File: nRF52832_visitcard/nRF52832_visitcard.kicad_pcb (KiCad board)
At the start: 4 copper layers, 91 x 50 mm, 67 parts, among them J1 Programming, J2 UART, SW1 SW_Push, Y1 32 MHz

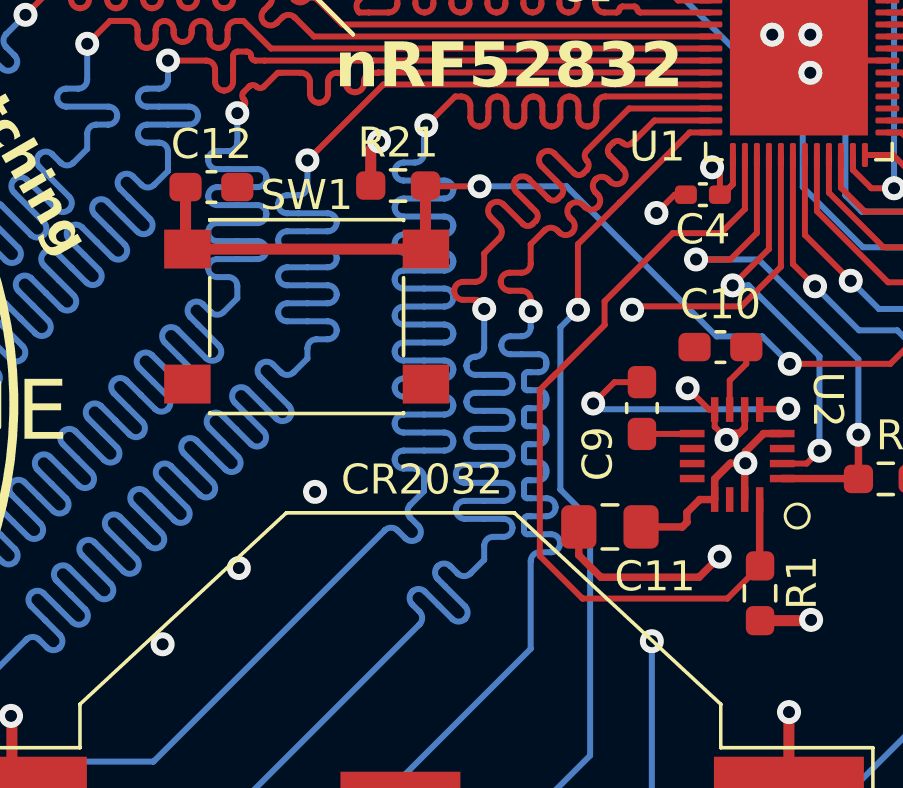
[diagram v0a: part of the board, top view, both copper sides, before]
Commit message: LCSC added to another component
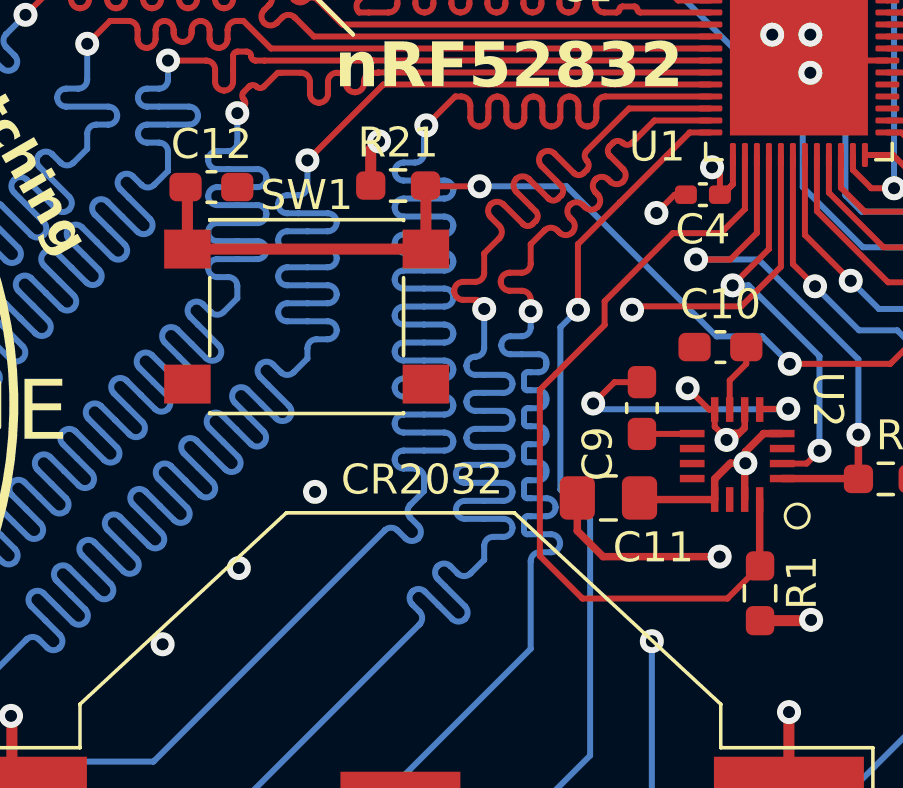
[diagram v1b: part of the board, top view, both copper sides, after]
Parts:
- moved C11 0.97 mm to (162.2, 108.2)
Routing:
- net VDD: track 43.7 -> 43.2 mm

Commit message: Board layout fix
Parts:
- removed the   at (116.9, 114.9)
- moved R2 8.53 mm to (163.3, 104.8), turned to 135 degrees
- moved R1 8.48 mm to (160.7, 105.9), turned to 180 degrees
- moved C9 8.20 mm to (171.1, 107.5)
- moved C10 6.45 mm to (169.4, 108.5), turned to -90 degrees
- moved C11 0.90 mm to (162.9, 108.7), turned to -90 degrees
- moved U2 0.68 mm to (166.3, 107.4), turned to 0 degrees
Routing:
- net /SCL: track 27.7 -> 16.0 mm
- net /SDA: track 18.3 -> 11.6 mm, vias 2 -> 0
- net /SETC: track 9.47 -> 3.23 mm, vias 2 -> 0
- net /SETP: track 1.68 -> 6.86 mm
- net GND: track 47.5 -> 43.7 mm, vias 91 -> 90
- net /D12: track 118.4 -> 115.8 mm
- net VDD: track 43.2 -> 44.3 mm
- net Net-(U2-C1): track 2.31 -> 1.50 mm
- net /PB: track 39.7 -> 39.2 mm
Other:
- board text removed: "+38766170888"
- board text removed: "Co-Founder"
- board text removed: "damjan.prerad@indigoingenium.ba"
- board text removed: "https://indigoingenium.ba"

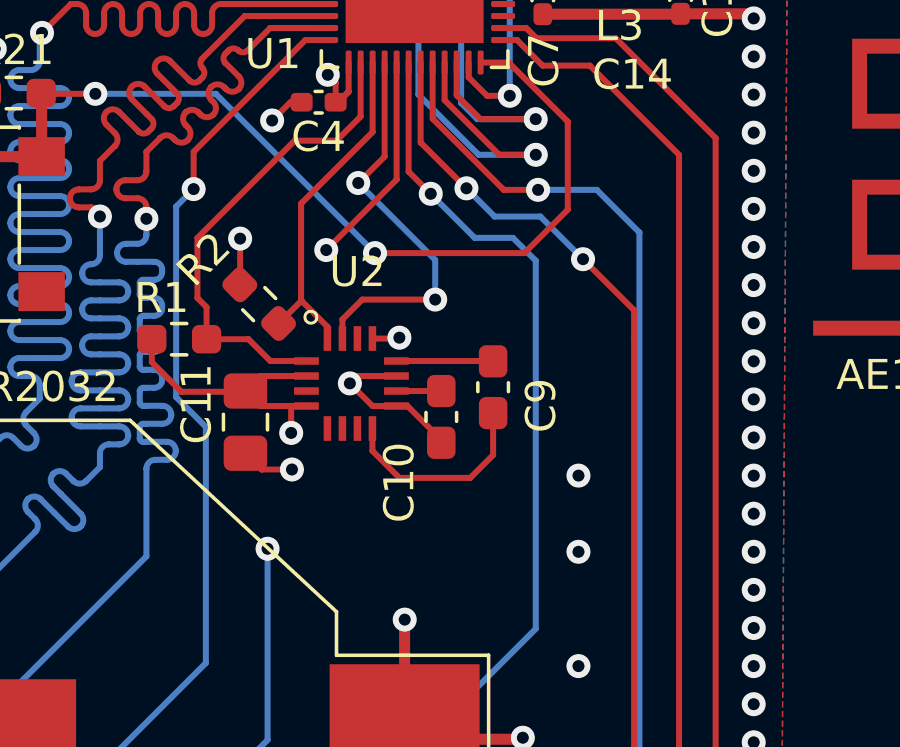
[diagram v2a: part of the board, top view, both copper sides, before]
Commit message: Using QMC5833L instead of HMC5883L
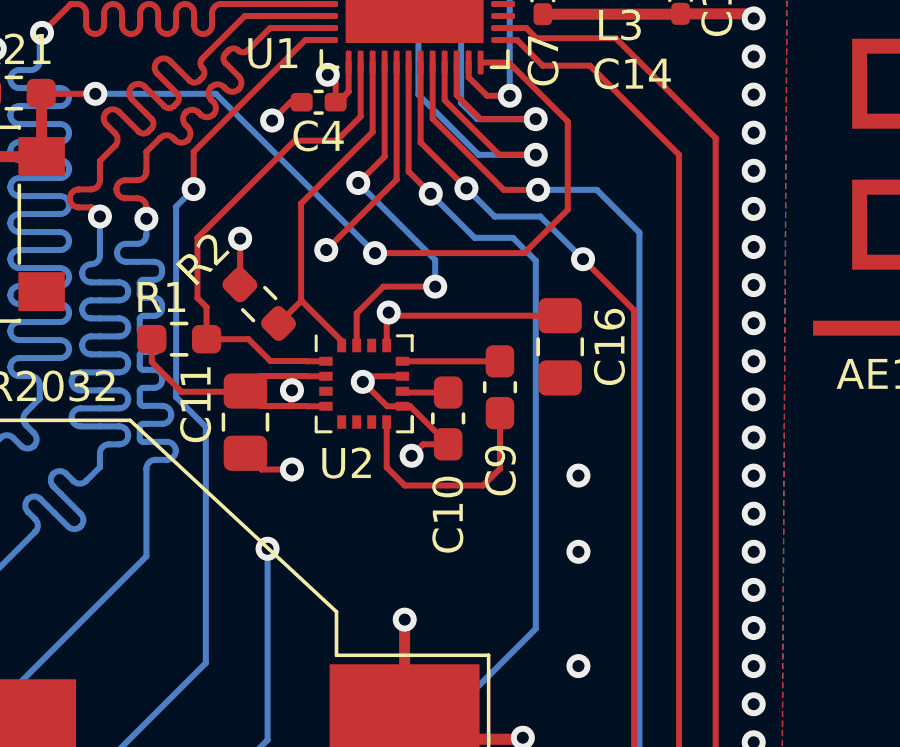
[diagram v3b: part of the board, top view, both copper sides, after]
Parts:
- added C16: 100n, Capacitor_SMD:C_0805_2012Metric_Pad1.18x1.45mm_HandSolder, F.Cu at (173.4, 106.2)
- U2: footprint HMC5883L:HMC5883L -> Package_LGA:LGA-16_3x3mm_P0.5mm
- moved U2 0.51 mm to (166.8, 107.4)
- moved C10 0.23 mm to (169.6, 108.6)
- moved C9 0.23 mm to (171.4, 107.5)
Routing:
- net VDD: track 44.3 -> 51.7 mm
- net GND: track 43.7 -> 44.6 mm, vias 90 -> 91
- net /SETP: track 6.86 -> 7.62 mm
- net /SCL: track 16.0 -> 16.7 mm
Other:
- board text added: "Bluetooth compass"
- board text added: "damjanovmail@gmail.com"
- board text removed: "INDIGO INGENUM"

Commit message: PCB details - Rotated battery holder in 3D view - Silkscreen fix
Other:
- board text added: "UART"
- board text removed: "Linux Bare-Metal"
- board text removed: "Python C / C++"
- board text removed: "Software and firmawre development PCB design and layout"
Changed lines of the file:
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@@
 (kicad_pcb (version 20221018) (generator pcbnew)
   (general
-    (thickness 0.19)
+    (thickness 1.5)
   )
   (paper "A4")
@@
       (layer "F.Mask" (type "Top Solder Mask") (thickness 0.01))
       (layer "F.Cu" (type "copper") (thickness 0.035))
-      (layer "dielectric 1" (type "prepreg") (thickness 0.01) (material "FR4") (epsilon_r 4.5) (loss_tangent 0.02))
+      (layer "dielectric 1" (type "prepreg") (thickness 0.1) (material "FR4") (epsilon_r 4.5) (loss_tangent 0.02))
       (layer "In1.Cu" (type "copper") (thickness 0.035))
-      (layer "dielectric 2" (type "core") (thickness 0.01) (material "FR4") (epsilon_r 4.5) (loss_tangent 0.02))
+      (layer "dielectric 2" (type "core") (thickness 1.14) (material "FR4") (epsilon_r 4.5) (loss_tangent 0.02))
       (layer "In2.Cu" (type "copper") (thickness 0.035))
-      (layer "dielectric 3" (type "prepreg") (thickness 0.01) (material "FR4") (epsilon_r 4.5) (loss_tangent 0.02))
+      (layer "dielectric 3" (type "prepreg") (thickness 0.1) (material "FR4") (epsilon_r 4.5) (loss_tangent 0.02))
       (layer "B.Cu" (type "copper") (thickness 0.035))
       (layer "B.Mask" (type "Bottom Solder Mask") (thickness 0.01))
@@
     (pad "2" smd rect (at 0 0 180) (size 4 4) (layers "F.Cu" "F.Paste" "F.Mask")
       (net 3 "GND") (pinfunction "-") (pintype "passive"))
-    (model "${KICAD7_3DMODEL_DIR}/Battery.3dshapes/BatteryHolder_Multicomp_BC-2001_1x2032.wrl"
-      (offset (xyz 0 0 0))
-      (scale (xyz 1 1 1))
-      (rotate (xyz 0 0 0))
-    )
     (model ":KICAD7_3DMODEL_DIR:Battery.3dshapes/BatteryHolder_Keystone_3034_1x20mm.wrl"
       (offset (xyz 0 0 0))
       (scale (xyz 1 1 1))
-      (rotate (xyz 0 0 0))
+      (rotate (xyz 0 0 180))
     )
   )
@@
   (gr_line (start 171.45 81.28) (end 173.99 83.82)
     (stroke (width 0.15) (type default)) (layer "F.SilkS"))
-  (gr_line (start 176.4538 83.0072) (end 175.2346 83.0072)
-    (stroke (width 0.15) (type default)) (layer "F.SilkS"))
   (gr_circle (center 127.3584 105.0254) (end 129.8584 105.0254)
     (stroke (width 0.15) (type default)) (fill none) (layer "F.SilkS"))
@@
   (gr_line (start 127.3584 105.0254) (end 124.8584 105.0254)
     (stroke (width 0.15) (type default)) (layer "F.SilkS"))
-  (gr_line (start 176.53 85.09) (end 175.26 85.09)
-    (stroke (width 0.15) (type default)) (layer "F.SilkS"))
   (gr_circle (center 127.3584 105.0254) (end 142.3584 105.0254)
     (stroke (width 0.3) (type default)) (fill none) (layer "F.SilkS"))
@@
     (effects (font (size 1 1) (thickness 0.15)) (justify left bottom))
   )
-  (gr_text "Linux\nBare-Metal" (at 176.53 86.36) (layer "F.SilkS")
+  (gr_text "UART" (at 174.7012 84.7598) (layer "F.SilkS")
     (effects (font (size 1.5 1.5) (thickness 0.3) bold) (justify left bottom))
   )
@@
     (effects (font (size 1 1) (thickness 0.15)) (justify left bottom))
   )
-  (gr_text "Python\nC / C++" (at 115.57 127) (layer "F.SilkS")
-    (effects (font (size 1.5 1.5) (thickness 0.3) bold) (justify left bottom))
-  )
   (gr_text "270\n" (at 128.7526 108.077 180) (layer "F.SilkS")
     (effects (font (size 1 1) (thickness 0.15)) (justify left bottom))
@@
     (effects (font (size 1 1) (thickness 0.15)) (justify left bottom mirror))
   )
-  (gr_text "Software and firmawre development\nPCB design and layout" (at 113.03 86.36) (layer "F.SilkS")
+  (gr_text "Bluetooth compass" (at 113.03 86.36) (layer "F.SilkS")
     (effects (font (size 1.5 1.5) (thickness 0.3) bold) (justify left bottom))
   )
